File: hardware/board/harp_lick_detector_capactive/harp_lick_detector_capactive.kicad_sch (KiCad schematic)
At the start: 77 parts, among them U1 ADA4807-4

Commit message: assign sch components partial
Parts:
- removed C? (x5): 100pF, symbol Device:C
- removed C?: 383pF, symbol Device:C
- removed C?: 1nF, symbol Device:C
- removed D?: BZV55B3V3, Diode_SMD:D_MiniMELF, symbol Diode:BZV55B3V3
- removed D?: ESD9B5.0ST5G, Diode_SMD:D_SOD-923, symbol Diode:ESD9B5.0ST5G
- removed J?: Conn_01x02_Female, symbol Connector:Conn_01x02_Female
- removed R?: 1M13, symbol Device:R
- removed R? (x3): 4K7, symbol Device:R
- removed R?: 100K, symbol Device:R
- removed R?: 300K, symbol Device:R
- removed R?: 9K76, symbol Device:R
- removed R?: 402, symbol Device:R
- removed R?: 10K, symbol Device:R
- removed R? (x2): 316K, symbol Device:R
- removed R?: 226, symbol Device:R
- removed R?: 634K, symbol Device:R
- removed R?: 6K19, symbol Device:R
- removed U? (x7): ADA4807-4, symbol Amplifier_Operational:ADA4807-4
- added J3: (no value), symbol Connector:Conn_Coaxial
- added R?: (no value), symbol Device:R
- C?: Link (none) -> https://www.digikey.com/en/products/detail/samsung-electro-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; Manufacturer (none) -> Samsung Electro-Mechanics; Manufacturer Number (none) -> CL10B105KA8NNNC; Rated Voltage (none) -> 25V; Temperature Coefficient (none) -> X7R
- C?: value 3.3uF -> (none)
- C?: value 1nF -> (none)
- C?: Link (none) -> https://www.digikey.com/en/products/detail/samsung-electro-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; Manufacturer Number (none) -> CL31A226KAHNNNE; Rated Voltage (none) -> 25V; Temperature Coefficient (none) -> X5R
- C? (x2): Link (none) -> https://www.digikey.com/en/products/detail/murata-electroni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; Manufacturer (none) -> Murata Electronics; Manufacturer Number (none) -> GRM188Z71E225KE43D; Rated Voltage (none) -> 25V; Temperature Coefficient (none) -> X7R
- C?: value 100pF -> (none); Link (none) -> https://www.digikey.com/en/products/detail/murata-electroni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; Manufacturer (none) -> Murata Electronics; Manufacturer Number (none) -> GRM033R71E101JA01D; Rated Voltage (none) -> 25V; Temperature Coefficient (none) -> X7R; Tolerance (none) -> 5%
- C?: Link (none) -> https://www.digikey.com/en/products/detail/murata-electroni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; Manufacturer (none) -> Murata Electronics; Manufacturer Number (none) -> GRM21BZ71E106KE15L; Rated Voltage (none) -> 25V; Temperature Coefficient (none) -> X7R
- C?: Link (none) -> https://www.digikey.com/en/products/detail/murata-electroni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; Manufacturer (none) -> Murata Electronics; Manufacturer Number (none) -> GRM21BZ71H475KE15K; Rated Voltage (none) -> 50V; Temperature Coefficient (none) -> X7R
- C? (x2): value 10nF -> (none)
- D?: value BZV55B3V3 -> (none); footprint Diode_SMD:D_MiniMELF -> (none)
- J1: renamed from J?; value Conn_01x03_Female -> (none)
- J5: renamed from J?; value Barrel_Jack_Switch_Pin3Ring -> (none)
- R12, R14: value 51K -> (none)
- R? (x2): value 160K -> (none)
- R? (x2): value 10K -> (none); footprint Resistor_SMD:R_0402_1005Metric_Pad0.72x0.64mm_HandSolder -> (none)
- R?: value 6K19 -> (none)
- R? (x4): value ??? -> (none)
- R?: value 9K76 -> (none)
- R? (x2): value 1M -> (none)
- R? (x2): value 4K7 -> (none)
- R?: value 60.4 -> (none)
- RN1: renamed from RN?; Link (none) -> https://www.digikey.com/en/products/detail/analog-devices-i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; Manufacturer (none) -> Analog Devices Inc.; Manufacturer Number (none) -> LT5400BIMS8E-5#PBF; Notes (none) -> ±0.025% resistor matching ratio
- U1: renamed from U?; Manufacturer (none) -> Texas Instruments; Manufacturer Number (none) -> INA849DR
- U2: renamed from U1; value ADA4807-4 -> (none)
- U2: renamed from U?; value ADA4807-4 -> (none)
- U6: renamed from U?; value LM27762 -> (none); footprint Package_SON:WSON-12-1EP_3x2mm_P0.5mm_EP1x2.65_ThermalVias -> (none)
- gave numbers to parts that had none: 2
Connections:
- net 100[Khz], 50[uVpp] Sine Wave Source1/VSIN: now also J3.1 (In)
- net GND: now also J3.2 (Ext)
- net at J4.1 (In), R?.2, RV?.2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: now also R?.2
- net at R?.2, RV?.1, U2.2 (-): now also R?.1
- no-connect marks 3 -> 2
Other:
- removed sheet 100[Khz], 100[mVpp] Sine Wave Source
- note added: "1M Wheatstone Bridge"
- note added: "DNP: Fixed Gain Resistor"
- note added: "SMB Raw Sine"
- note removed: "-0.1sin(2π100000t)"
- note removed: "1.65 + 1.65sin(2π100000t)"
- note removed: "100[Khz] Inverting Bandpass Filter 2 Pole Bessel"
- note removed: "100[Khz] Non-Inverting Bandpass Filter"
- note removed: "200 + 180 in parallel"
- note removed: "2nd Order Chebyshev Filter Fc = 100KHz"
- note removed: "3.3sin(2π100000t)"
- note removed: "ADA4807: * Rail to Rail * Low noise"
- note removed: "Buffer"
- note removed: "External Lick Input Self-Capacitance Measurement Model"
- note removed: "Highpass Filter Fc = 30KHz"
- note removed: "Input Capacitance is 3[pF]"
- note removed: "Inverting Amplifer G = 30"
- note removed: "Mouse body: <100pF"
- note removed: "OR: 10[MHz], ~8-14 bit ADC via parallel Options: MAX19191, MAX1426"
- note removed: "OR: RMS-to-DC converter Option: AD736 Option: Full Wave Precision Rectifier + lowpass filter"
- note removed: "TODO: 1-2[MHz], ~8-14 bit ADC via SPI Options: ADS7056, ADS7029-Q1"
- note removed: "TODO: 5-10x non-inverting amplifier here. 12K/1.5K in lab."
- note removed: "TODO: SMB raw analog output signal."
- note removed: "TODO: consider SMB input signal."
- note removed: "Wet Tongue + Brain: ~1K"
- note removed: "Wheatstone Bridge"
- moved on the sheet: C?, R?, U1, U2B, U2D

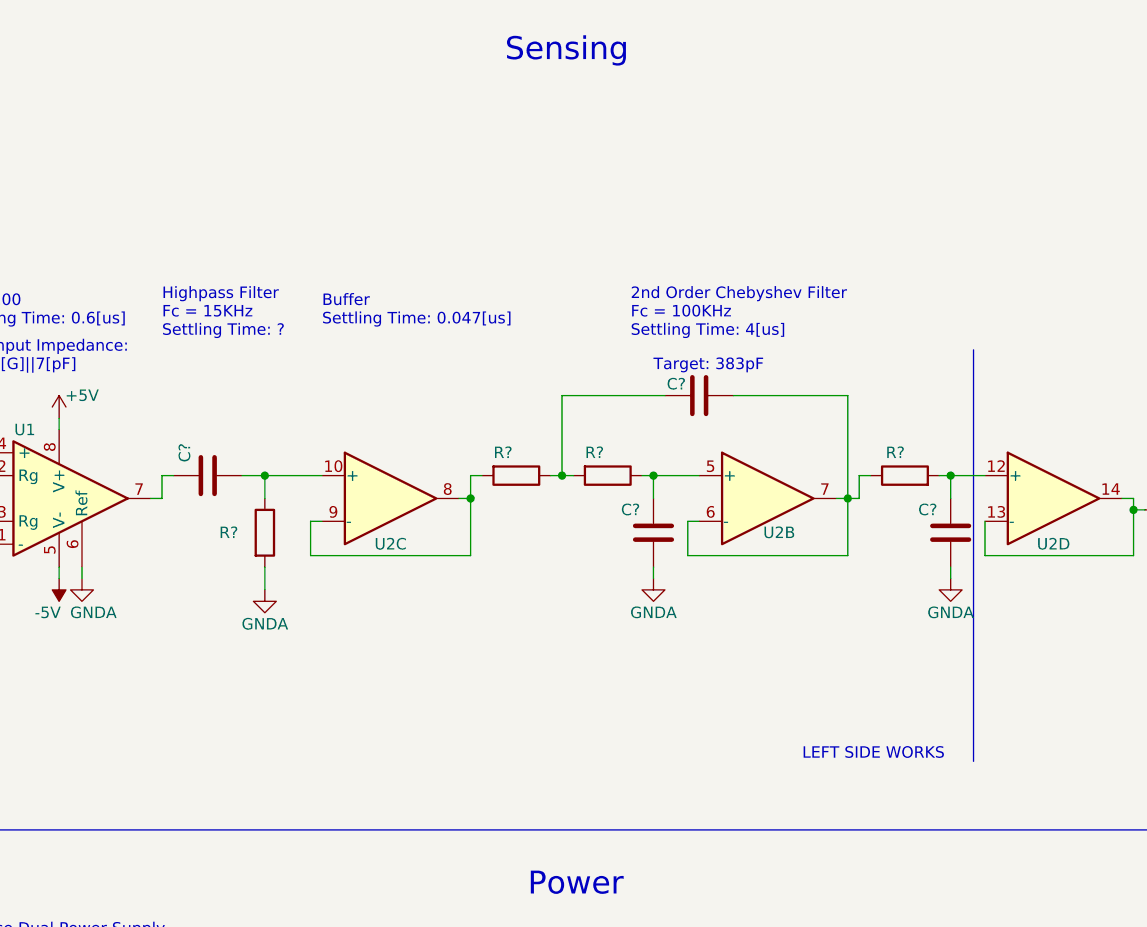
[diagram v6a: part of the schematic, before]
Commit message: assign more sch components
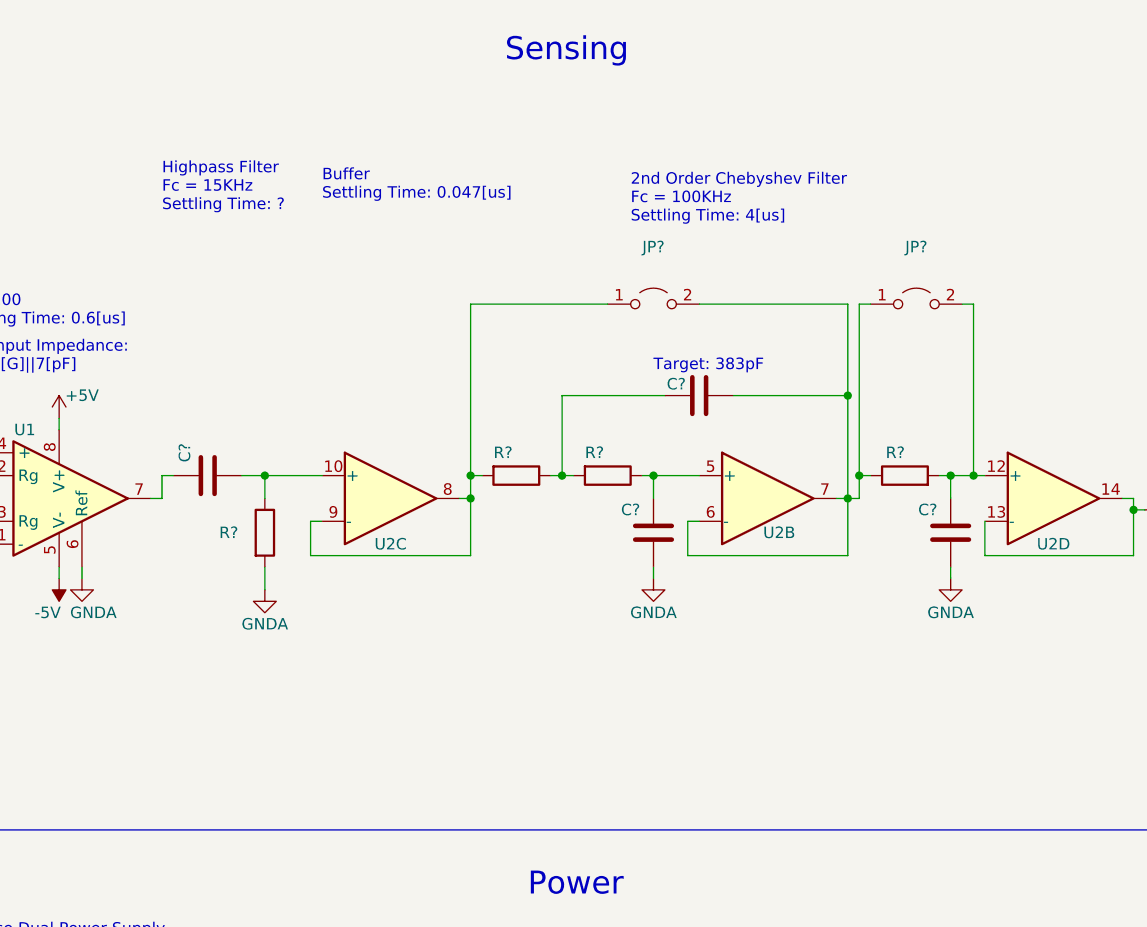
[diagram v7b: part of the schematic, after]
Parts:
- removed C?: (no value), symbol Device:C
- added C?: (no value), symbol Device:C
- added JP? (x2): (no value), symbol Jumper:Jumper_2_Open
- C?: Link (none) -> https://www.digikey.com/en/products/detail/tdk-corporation/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; Manufacturer (none) -> TDK Corporation; Manufacturer Number (none) -> CGA4J1X7R1E335K125AC; Rated Voltage (none) -> 25V; Temperature Coefficient (none) -> X7R; Tolerance (none) -> 10%
- C?: Link (none) -> https://www.digikey.com/en/products/detail/kemet/C0603C102J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; Manufacturer (none) -> Kemet; Manufacturer Number (none) -> C0603C102J5RAC7411; Rated Voltage (none) -> 50V; Temperature Coefficient (none) -> X7R; Tolerance (none) -> 5%
- C?: Tolerance (none) -> 10%
- C? (x2): Link (none) -> https://www.digikey.com/en/products/detail/kemet/C0603X103J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; Manufacturer (none) -> Kemet; Manufacturer Number (none) -> C0603X103J5RECAUTO; Rated Voltage (none) -> 50V; Temperature Coefficient (none) -> X7R; Tolerance (none) -> 5%
- J1: Link (none) -> https://www.digikey.com/en/products/detail/phoenix-contact/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; Manufacturer (none) -> Phoenix Contact; Manufacturer Number (none) -> 1844223
- J3, J4: Link (none) -> https://www.digikey.com/en/products/detail/amphenol-rf/901-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; Manufacturer (none) -> Amphenol RF; Manufacturer Number (none) -> 901-143-6RFX
- R12, R14: Link (none) -> https://www.digikey.com/en/products/detail/panasonic-electr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; Manufacturer (none) -> Panasonic Electronic Components; Manufacturer Number (none) -> ERJ-UP3F5102V; Tolerance (none) -> 1%
- R? (x2): Link (none) -> https://www.digikey.com/en/products/detail/te-connectivity-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; Manufacturer (none) -> TE Connectivity Passive Product; Manufacturer Number (none) -> CRGP0603F390R; Tolerance (none) -> 1%
- U2: Link (none) -> https://www.digikey.com/en/products/detail/analog-devices-i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; Manufacturer (none) -> Analog Devices Inc.; Manufacturer Number (none) -> ADA4807-4ARUZ-R7
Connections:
- net GND: now also C?.2
- net at R?.2, U2.8, U2.9 (-): now also JP?.1 (A)
- net at C?.1, R?.1, U2.6 (-)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: now also JP?.1 (A), JP?.2 (B)
- net at R?.2, U2.12 (+): now also C?.1, JP?.2 (B)
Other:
- note removed: "LEFT SIDE WORKS"

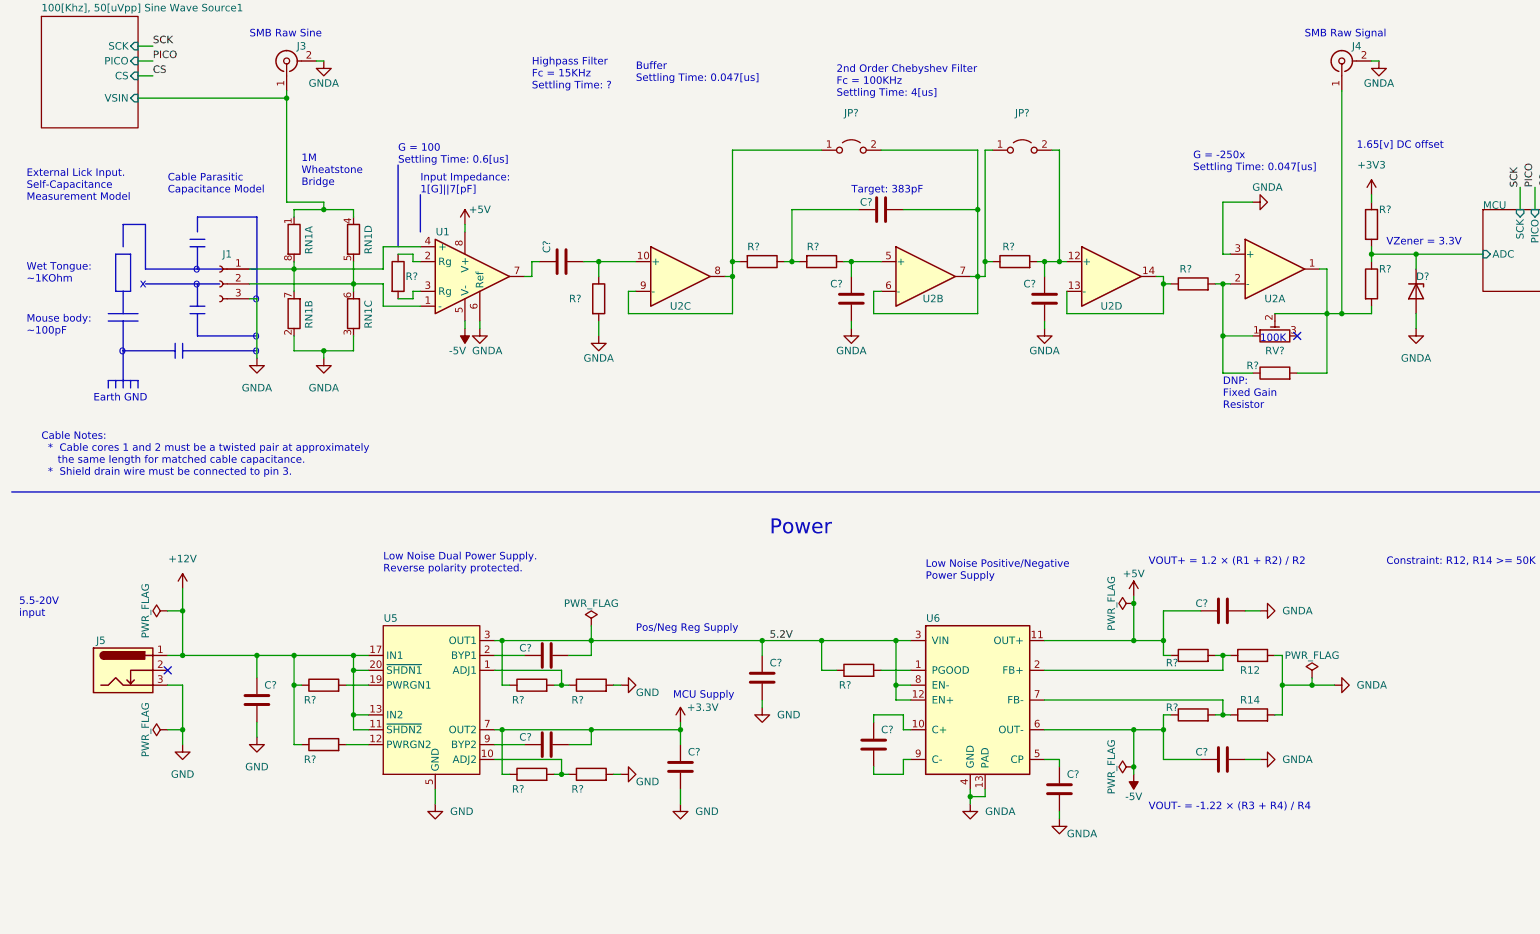
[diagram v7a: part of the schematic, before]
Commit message: assign more components
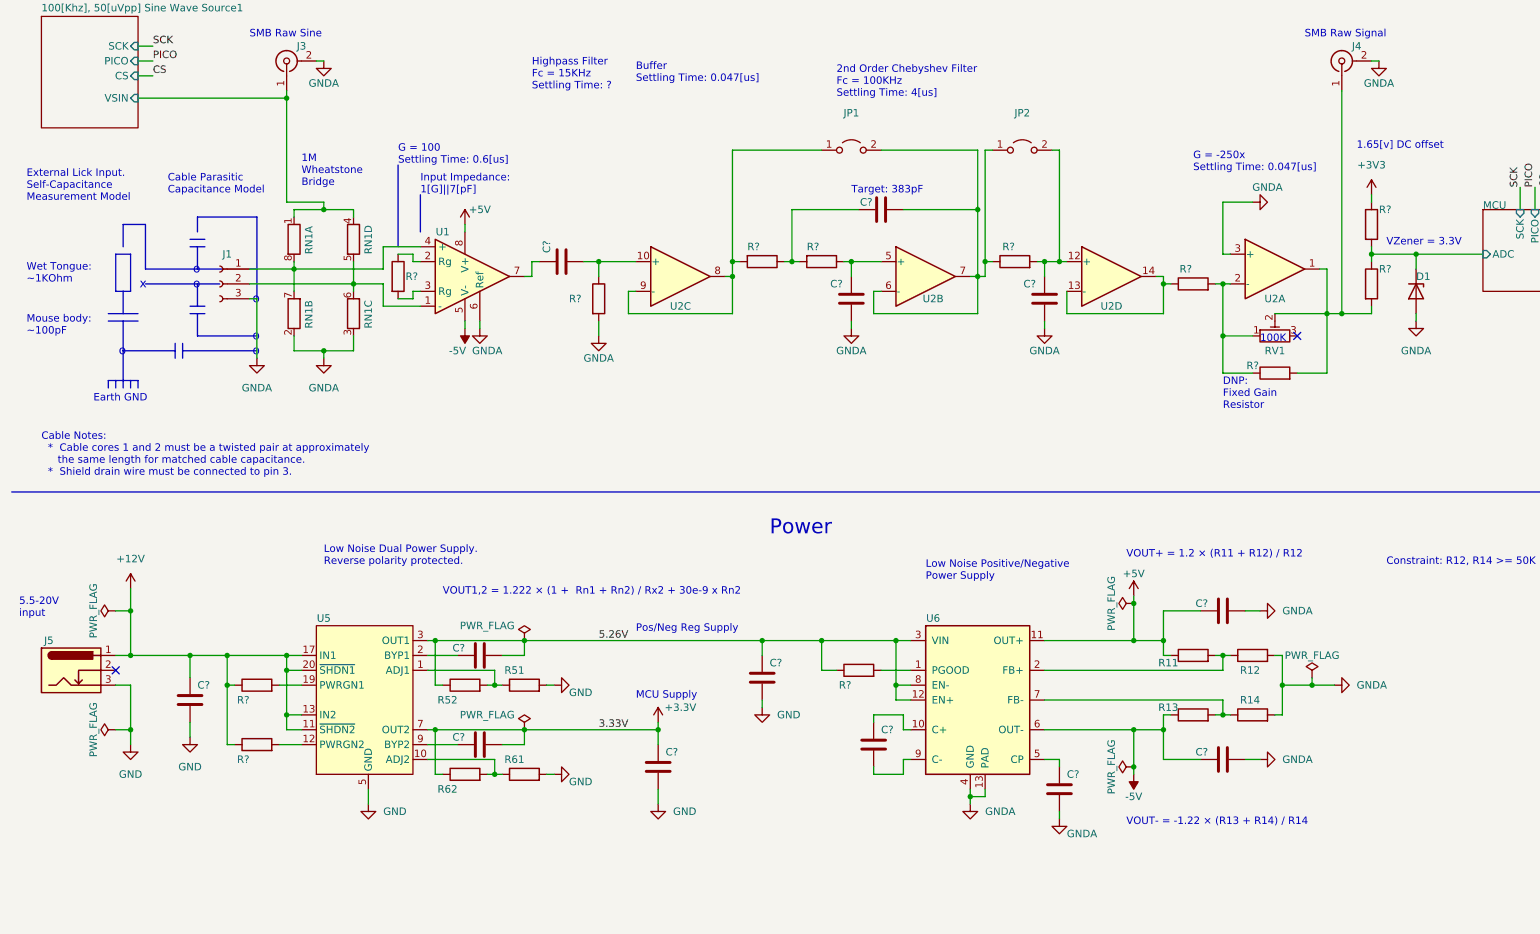
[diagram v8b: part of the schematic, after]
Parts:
- D1: renamed from D?; Link (none) -> https://www.mouser.com/ProductDetail/Nexperia/BZX384-A3V3-Q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; Manufacturer (none) -> Nexperia; Manufacturer Number (none) -> BZX384-A3V3-QX; Tolerance (none) -> 1%
- R11, R13: renamed from R?; Link (none) -> https://www.digikey.com/en/products/detail/panasonic-electr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; Manufacturer (none) -> Panasonic Electronic Components; Manufacturer Number (none) -> ERJ-UP3F1603V; Tolerance (none) -> 1%
- R51, R61: renamed from R?; Link (none) -> https://www.digikey.com/en/products/detail/te-connectivity-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; Manufacturer (none) -> TE Connectivity Passive Product; Manufacturer Number (none) -> CRGP0603F100K
- R52: renamed from R?; Link (none) -> https://www.digikey.com/en/products/detail/te-connectivity-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; Manufacturer (none) -> TE Connectivity Passive Product; Manufacturer Number (none) -> CRGP0603F330K; Tolerance (none) -> 1%
- R62: renamed from R?; Link (none) -> https://www.digikey.com/en/products/detail/stackpole-electr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; Manufacturer (none) -> Stackpole Electronics Inc.; Manufacturer Number (none) -> RNCF0603BKE172K; Tolerance (none) -> 0.1%
- R? (x3): Manufacturer (none) -> KOA Speer Electronics, Inc.; Manufacturer Number (none) -> SG73P1EWTTP1002F
- R? (x2): Link (none) -> https://www.digikey.com/en/products/detail/te-connectivity-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; Manufacturer (none) -> TE Connectivity Passive Product; Manufacturer Number (none) -> CRGP0603F1M0; Tolerance (none) -> 1%
- R? (x2): Link (none) -> https://www.digikey.com/en/products/detail/te-connectivity-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; Manufacturer (none) -> TE Connectivity Passive Product; Manufacturer Number (none) -> CRGP0603F4K7; Tolerance (none) -> 1%
- R?: Link (none) -> https://www.digikey.com/en/products/detail/rohm-semiconduct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; Manufacturer (none) -> Rohm Semiconductor; Manufacturer Number (none) -> ESR03EZPD60R4; Tolerance (none) -> 0.5%
- RV1: renamed from RV?; Link (none) -> https://www.digikey.com/en/products/detail/bourns-inc/3314G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; Manufacturer (none) -> Bourns Inc.; Manufacturer Number (none) -> 3314G-2-104E
- gave numbers to parts that had none: 2
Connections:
- net 5.2V renamed 5.26V
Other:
- note added: "VOUT+ = 1.2 × (R11 + R12) / R12"
- note added: "VOUT- = -1.22 × (R13 + R14) / R14"
- note added: "VOUT1,2 = 1.222 × (1 + Rn1 + Rn2) / Rx2 + 30e-9 x Rn2"
- note removed: "VOUT+ = 1.2 × (R1 + R2) / R2"
- note removed: "VOUT- = -1.22 × (R3 + R4) / R4"
- moved on the sheet: C?, J5, R51, R52, R61, R62, R?, U5
